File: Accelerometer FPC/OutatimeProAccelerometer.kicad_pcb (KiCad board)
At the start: 2 copper layers, 12.4 x 7.3 mm, 5 parts, among them J1 FH35C-9S-0.3SHW, U1 LIS2DW12TR

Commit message: v270826: change programming header, add test points
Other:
- board text added: "Outatime Pro LIS2DW12TR v270826"
- board text removed: "Outatime Pro LIS2DW12TR v250826"
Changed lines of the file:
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@@
 		(capping no)
 		(filling no)
-		(zone_defaults)
 		(grid_origin 25.25 21.35)
 		(pcbplotparams
@@
 		(layer "User.4")
 	)
-	(gr_text "Outatime Pro\nLIS2DW12TR\n\nv250826"
+	(gr_text "Outatime Pro\nLIS2DW12TR\n\nv270826"
 		(at 14.5 14.65 0)
 		(layer "F.SilkS")
@@
 	)
 	(zone
+		(net "VCC")
+		(layer "F.Cu")
+		(hatch none 0.1)
+		(priority 30000)
+		(attr
+			(teardrop
+				(type padvia)
+			)
+		)
+		(connect_pads yes
+			(clearance 0)
+		)
+		(min_thickness 0.0254)
+		(fill yes
+			(island_removal_mode 1)
+		)
+		(polygon
+			(pts
+				(xy 23.617457 16.023964) (xy 23.476036 15.882543) (xy 23.057697 16.095543) (xy 23.192486 16.307514)
+				(xy 23.404457 16.442303)
+			)
+		)
+	)
+	(zone
 		(net "GND")
 		(layer "F.Cu")
@@
 	)
 	(zone
-		(net "VCC")
+		(net "/A3_INT2")
 		(layer "F.Cu")
 		(hatch none 0.1)
-		(priority 30000)
+		(priority 30002)
 		(attr
 			(teardrop
@@
 		(polygon
 			(pts
-				(xy 23.617457 16.023964) (xy 23.476036 15.882543) (xy 23.057697 16.095543) (xy 23.192486 16.307514)
-				(xy 23.404457 16.442303)
+				(xy 22.070679 16.151248) (xy 22.070679 16.001248) (xy 21.625002 15.875) (xy 21.619679 16.076248)
+				(xy 21.763278 16.277496)
 			)
 		)
@@
 	)
 	(zone
-		(net "/A3_INT2")
-		(layer "F.Cu")
+		(net "VCC")
+		(layer "B.Cu")
 		(hatch none 0.1)
 		(priority 30002)
@@
 		(polygon
 			(pts
-				(xy 22.070679 16.151248) (xy 22.070679 16.001248) (xy 21.625002 15.875) (xy 21.619679 16.076248)
-				(xy 21.763278 16.277496)
+				(xy 18.825 15.95) (xy 19.025 15.95) (xy 19.357873 15.361104) (xy 18.925 15.024) (xy 18.492127 15.361104)
 			)
 		)
@@
 		(layer "B.Cu")
 		(hatch none 0.1)
-		(priority 30001)
+		(priority 30008)
 		(attr
 			(teardrop
@@
 		(polygon
 			(pts
-				(xy 17.275 15.95) (xy 17.475 15.95) (xy 17.807873 15.361104) (xy 17.375 15.024) (xy 16.942127 15.361104)
+				(xy 24.554804 15.63) (xy 24.554804 15.83) (xy 25.05 15.95) (xy 25.055804 15.73) (xy 24.887519 15.51)
 			)
 		)
@@
 	)
 	(zone
-		(net "GND")
+		(net "VCC")
 		(layer "B.Cu")
 		(hatch none 0.1)
-		(priority 30009)
+		(priority 30000)
 		(attr
 			(teardrop
@@
 		(polygon
 			(pts
-				(xy 20.744688 16.75) (xy 20.744688 16.55) (xy 20.45 16.45) (xy 20.243688 16.65) (xy 20.25 16.85)
+				(xy 19.825 15.125) (xy 19.825 14.925) (xy 19.247887 14.575) (xy 18.924 15.025) (xy 19.247887 15.475)
 			)
 		)
 	)
 	(zone
-		(net "/A3_INT2")
+		(net "VCC")
 		(layer "B.Cu")
 		(hatch none 0.1)
-		(priority 30015)
+		(priority 30005)
 		(attr
 			(teardrop
@@
 		(polygon
 			(pts
-				(xy 25 18.8) (xy 24.9 18.8) (xy 24.85 18.9) (xy 24.95 19.251) (xy 25.05 18.9)
+				(xy 24.715 14.87) (xy 24.715 14.67) (xy 24.348576 14.500657) (xy 24.124 14.77) (xy 24.348576 15.039343)
 			)
 		)
@@
 		(layer "B.Cu")
 		(hatch none 0.1)
-		(priority 30002)
+		(priority 30004)
 		(attr
 			(teardrop
@@
 		(polygon
 			(pts
-				(xy 18.825 15.95) (xy 19.025 15.95) (xy 19.357873 15.361104) (xy 18.925 15.024) (xy 18.492127 15.361104)
+				(xy 23.535 14.67) (xy 23.535 14.87) (xy 23.901424 15.039343) (xy 24.126 14.77) (xy 23.901424 14.500657)
 			)
 		)
 	)
 	(zone
-		(net "VCC")
+		(net "GND")
 		(layer "B.Cu")
 		(hatch none 0.1)
-		(priority 30012)
+		(priority 30011)
 		(attr
 			(teardrop
@@
 		(polygon
 			(pts
-				(xy 24.125 18.775) (xy 23.925 18.775) (xy 23.9 18.9) (xy 24.025 19.251) (xy 24.15 18.9)
+				(xy 17.475 16.448002) (xy 17.275 16.448002) (xy 17.275 16.625) (xy 17.304289 16.695711) (xy 17.354804 16.898773)
+				(xy 17.604104 16.854104) (xy 17.648773 16.604804) (xy 17.445711 16.554289)
 			)
 		)
 	)
 	(zone
-		(net "VCC")
+		(net "/A3_INT2")
 		(layer "B.Cu")
 		(hatch none 0.1)
-		(priority 30006)
+		(priority 30010)
 		(attr
 			(teardrop
@@
 		(polygon
 			(pts
-				(xy 22.75324 16.05) (xy 22.75324 16.25) (xy 23.057697 16.511277) (xy 23.25424 16.15) (xy 23.245363 16.058214)
+				(xy 21.675 15.654323) (xy 21.525 15.654323) (xy 21.400002 16.1) (xy 21.6 16.105323) (xy 21.799998 15.958574)
 			)
 		)
@@
 	)
 	(zone
-		(net "GND")
+		(net "VCC")
 		(layer "B.Cu")
 		(hatch none 0.1)
-		(priority 30003)
+		(priority 30006)
 		(attr
 			(teardrop
@@
 		(polygon
 			(pts
-				(xy 24.715 15.83) (xy 24.715 15.63) (xy 24.348576 15.460657) (xy 24.124 15.73) (xy 24.348576 15.999343)
+				(xy 22.75324 16.05) (xy 22.75324 16.25) (xy 23.057697 16.511277) (xy 23.25424 16.15) (xy 23.245363 16.058214)
 			)
 		)
 	)
 	(zone
-		(net "/SDA")
+		(net "GND")
 		(layer "B.Cu")
 		(hatch none 0.1)
-		(priority 30014)
+		(priority 30003)
 		(attr
 			(teardrop
@@
 		(polygon
 			(pts
-				(xy 25.925 18.8) (xy 25.775 18.8) (xy 25.75 18.9) (xy 25.85 19.251) (xy 25.95 18.9)
+				(xy 24.715 15.83) (xy 24.715 15.63) (xy 24.348576 15.460657) (xy 24.124 15.73) (xy 24.348576 15.999343)
 			)
 		)
@@
 		(layer "B.Cu")
 		(hatch none 0.1)
-		(priority 30004)
-		(attr
-			(teardrop
-				(type padvia)
-			)
-		)
-		(connect_pads yes
-			(clearance 0)
-		)
-		(min_thickness 0.0254)
-		(fill yes
-			(island_removal_mode 1)
-		)
-		(polygon
-			(pts
-				(xy 23.535 14.67) (xy 23.535 14.87) (xy 23.901424 15.039343) (xy 24.126 14.77) (xy 23.901424 14.500657)
-			)
-		)
-	)
-	(zone
-		(net "/A3_INT2")
-		(layer "B.Cu")
-		(hatch none 0.1)
-		(priority 30010)
+		(priority 30012)
 		(attr
 			(teardrop
@@
 		(polygon
 			(pts
-				(xy 21.675 15.654323) (xy 21.525 15.654323) (xy 21.400002 16.1) (xy 21.6 16.105323) (xy 21.799998 15.958574)
+				(xy 24.125 18.775) (xy 23.925 18.775) (xy 23.9 18.9) (xy 24.025 19.251) (xy 24.15 18.9)
 			)
 		)
@@
 		(layer "B.Cu")
 		(hatch none 0.1)
-		(priority 30008)
+		(priority 30001)
 		(attr
 			(teardrop
@@
 		(polygon
 			(pts
-				(xy 24.554804 15.63) (xy 24.554804 15.83) (xy 25.05 15.95) (xy 25.055804 15.73) (xy 24.887519 15.51)
+				(xy 17.275 15.95) (xy 17.475 15.95) (xy 17.807873 15.361104) (xy 17.375 15.024) (xy 16.942127 15.361104)
 			)
 		)
 	)
 	(zone
-		(net "VCC")
+		(net "/A4_INT1")
 		(layer "B.Cu")
 		(hatch none 0.1)
-		(priority 30005)
+		(priority 30016)
 		(attr
 			(teardrop
@@
 		(polygon
 			(pts
-				(xy 24.715 14.87) (xy 24.715 14.67) (xy 24.348576 14.500657) (xy 24.124 14.77) (xy 24.348576 15.039343)
+				(xy 24.7 18.8) (xy 24.6 18.8) (xy 24.55 18.9) (xy 24.65 19.251) (xy 24.75 18.9)
 			)
 		)
 	)
 	(zone
-		(net "/A4_INT1")
+		(net "/A3_INT2")
 		(layer "B.Cu")
 		(hatch none 0.1)
-		(priority 30016)
+		(priority 30015)
 		(attr
 			(teardrop
@@
 		(polygon
 			(pts
-				(xy 24.7 18.8) (xy 24.6 18.8) (xy 24.55 18.9) (xy 24.65 19.251) (xy 24.75 18.9)
+				(xy 25 18.8) (xy 24.9 18.8) (xy 24.85 18.9) (xy 24.95 19.251) (xy 25.05 18.9)
 			)
 		)
 	)
 	(zone
-		(net "GND")
+		(net "/SDA")
 		(layer "B.Cu")
 		(hatch none 0.1)
-		(priority 30011)
+		(priority 30014)
 		(attr
 			(teardrop
@@
 		(polygon
 			(pts
-				(xy 17.475 16.448002) (xy 17.275 16.448002) (xy 17.275 16.625) (xy 17.304289 16.695711) (xy 17.354804 16.898773)
-				(xy 17.604104 16.854104) (xy 17.648773 16.604804) (xy 17.445711 16.554289)
+				(xy 25.925 18.8) (xy 25.775 18.8) (xy 25.75 18.9) (xy 25.85 19.251) (xy 25.95 18.9)
 			)
 		)
 	)
 	(zone
-		(net "VCC")
+		(net "GND")
 		(layer "B.Cu")
 		(hatch none 0.1)
-		(priority 30000)
+		(priority 30009)
 		(attr
 			(teardrop
@@
 		(polygon
 			(pts
-				(xy 19.825 15.125) (xy 19.825 14.925) (xy 19.247887 14.575) (xy 18.924 15.025) (xy 19.247887 15.475)
+				(xy 20.744688 16.75) (xy 20.744688 16.55) (xy 20.45 16.45) (xy 20.243688 16.65) (xy 20.25 16.85)
 			)
 		)

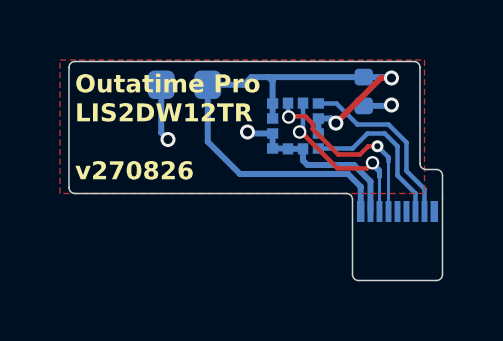
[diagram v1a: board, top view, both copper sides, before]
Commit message: move test pads more and change version format
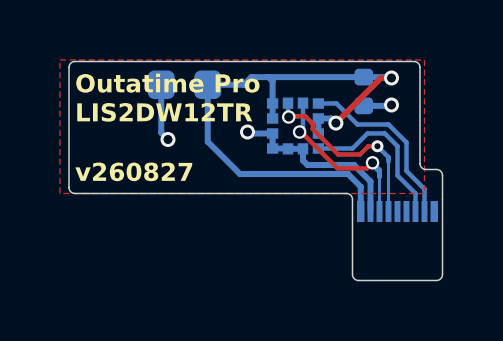
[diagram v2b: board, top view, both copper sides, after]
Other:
- board text added: "Outatime Pro LIS2DW12TR"
- board text added: "v260827"
- board text removed: "Outatime Pro LIS2DW12TR v270826"

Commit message: rename seg/com numbers to reflect firmware, fix up batt/vcc change circuitry
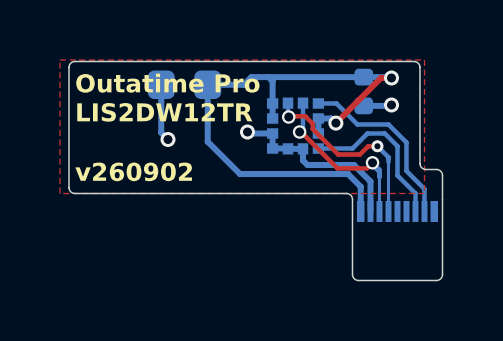
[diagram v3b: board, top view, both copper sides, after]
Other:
- board text added: "v260902"
- board text removed: "v260827"
